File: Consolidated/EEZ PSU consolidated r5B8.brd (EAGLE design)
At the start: 316 x 150 mm, 529 parts, among them IC1 LTC3864, IC10 REF5025, IC11 DAC8552, IC12 ADG465SOT-23, IC13 TS5A9411DCKT, IC14 ADS1120, IC15 LP339D, IC16 LM25575, IC17 MC7812, IC18 TPD4E002DRLR, IC19 TPD2E001DZDR, IC2 MC79L05, IC20 ADUM3160BRWZ, IC21 TLC5925IDBQR, IC22 Si8641EC-B-IS1, IC23 SI8651EC-B-IS1, IC24 SI8651EC-B-IS1, IC25 LD1117ADT33TR, IC26 Si8641EC-B-IS1, IC27 PCA21125, IC28 AT25256B, IC29 W5500, IC3 MC78L05, IC30 BC857BS, IC31 TLC555, IC32 SN74LVC2G08DCTR, IC33 TPS3705-33D, IC34 SN74LV1T34DBVR, IC35 SN74LVC2G02DCTR, IC4 LM5574, IC5 LP2951SO8, IC6 TL072D, IC7 TL072D, IC8 OP27GSZ, IC9 MCP23S08-E/SO, J1 BS-244DSM-R, J2 BS-244DSM-G, J3 BS-244DSM-B, J4 BS-244DSM-R, J5 BS-244DSM-B, Q1 SUD19P06-60, Q10 MMBT5401, Q11 MMBT5401, Q12 MMBT5551, Q13 MMBT5551, Q14 BSS84P, Q15 2N7002, Q16 MMBT5551, Q17 MMBT5401, Q18 MMBT5551, Q19 MMBT5551, Q2 MMBT5401, Q20 BTA26-600, Q21 BTA26-600, Q22 IRLL014N, Q23 IRLML2246TRPBF, Q24 IRLML2246TRPBF, Q25 IRLML2246TRPBF, Q26 IRLML2246TRPBF, Q27 2N7002, Q28 IRLML2246TRPBF, Q29 2N7002, Q3 2N7002, Q30 2N7002, Q4 IRFP250N, Q5 BC857C, Q6 BC846C, Q7 BCP56-16.115, Q8 IRFR5410, Q9 BCP56-16.115, SW1 A101SYCQ04, SW2 1301.9316, X1 282836-3, X10 826629-5, X11 2411-01, X12 MC000006, X13 TSW-113-07-F-D, X14 MC000005, X15 TSW-113-07-F-D, X16 09185067324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

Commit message: Consolidated PCB, jumpers renumbering
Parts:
- removed JMP1, JMP2: 0R-JUMPA, jump-0r-smd:A0R-JMP
- added JP6, JP7: 0R-JUMPA, jump-0r-smd:A0R-JMP
- C18: value EEEFK1J470P -> EEEFK1J101P
- D28: device diode:DO214AC -> EEZ_Lib1:SOD123
- FB6, FB7: value 2506033007Y3 -> 60R@100MHz
- JP1: value 826926-2 -> 0R-JUMPA; device jumper:JP1 -> jump-0r-smd:A0R-JMP
- JP3: value 0R-JUMPA -> 826926-2; device jump-0r-smd:A0R-JMP -> jumper:JP1
- L2: value See Note 1.2 -> 7443551331
- LED1: device led:CHIPLED_0805 -> EEZ_Lib1:LED_0805
- R12: value See Note 1.3 -> 324K
- moved JP2 301.9 mm to (15.5, 134.0), turned to 90 degrees
- moved JP1 128.8 mm to (107.6, 125.8), turned to 180 degrees
- moved JP3 80.8 mm to (224.2, 71.1), turned to 90 degrees
- moved JP4 24.5 mm to (307.8, 58.8)
- moved JP5 12.2 mm to (299.5, 42.0)
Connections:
- net !INT: now also JP2.2; no longer JMP2.2
- net !PS_DRDY: now also JP2.3; no longer JMP2.3
- net !PWD_RST: now also JP3.1; no longer JP1.1
- net +3V3: now also JP4.3; no longer JP2.3
- net +5V: now also JP4.1; no longer JP2.1
- net GND: now also JP3.2; no longer JP1.2
- net INT_EXP: now also JP2.1; no longer JMP2.1
- net MISO: now also JP7.1; no longer JP5.1
- net MODE: now also JP1.2; no longer JMP1.2
- net MOSI: now also JP6.1; no longer JP4.1
- net N$102: now also JP4.2; no longer JP2.2
- net N$104: now also JP7.2; no longer JP5.2
- net N$105: now also JP5.2; no longer JP3.2
- net N$106: now also JP6.2; no longer JP4.2
- net SCLK: now also JP5.1; no longer JP3.1
- net SGND: now also JP1.1; no longer JMP1.1
- net SYNC: now also JP1.3; no longer JMP1.3
- net TOUCH_DIN: now also JP6.3; no longer JP4.3
- net TOUCH_DOUT: now also JP7.3; no longer JP5.3
- net TOUCH_SCLK: now also JP5.3; no longer JP3.3
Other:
- board text added: "JP6"
- board text added: "JP7"
- board text removed: "JMP1"
- board text removed: "JMP2"

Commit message: Fixed fan control, miniMELF replaced with SOD-323
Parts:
- added C157: 100n, rcl:C0603
- added D29: SKL16, EEZ_Lib1:SOD123
- C104: value 470n/100V -> 100n; device rcl:C1812 -> rcl:C0603
- C105, C110: value 10n -> 470n/100V; device rcl:C1206 -> rcl:C1812
- C106, C111: value UPW1J150MED -> 10n; device MyLib6:CAPAE660X610N_COMBO2 -> rcl:C1206
- C107: value 10u -> UPW1J150MED; device rcl:C1206 -> MyLib6:CAPAE660X610N_COMBO2
- C108: value 10n -> 10u
- C109: value 470n/100V -> 10n; device rcl:C1812 -> rcl:C1206
- C112: value 10n -> UPW1J150MED; device rcl:C1206 -> MyLib6:CAPAE660X610N_COMBO2
- C113: value 100n -> 10n; device rcl:C0603 -> rcl:C1206
- C119: value 47u -> 100n; device MyLib6:PANASONIC_C -> rcl:C0603
- C120: value 10u -> 47u
- C121: value 100n -> 10u; device rcl:C0603 -> MyLib6:PANASONIC_C
- C125: value 10u -> 100n; device rcl:C1206 -> rcl:C0603
- C126: value 100n -> 10u; device rcl:C0603 -> rcl:C1206
- C127: value EECS5R5H105 -> 100n; device EEZ_Lib1:SG-R20MM -> rcl:C0603
- C128: value 100n -> EECS5R5H105; device rcl:C0603 -> EEZ_Lib1:SG-R20MM
- C130: value 22n -> 100n; device rcl:C0805 -> rcl:C0603
- C131: value 18p -> 22n
- C132: value 6n8 -> 18p; device rcl:C0603 -> rcl:C0805
- C133: value 10n -> 6n8; device rcl:C0805 -> rcl:C0603
- C134: value 6n8 -> 10n; device rcl:C0603 -> rcl:C0805
- C135: value 18p -> 6n8; device rcl:C0805 -> rcl:C0603
- C136: value 100n -> 18p; device rcl:C0603 -> rcl:C0805
- C144: value 10u -> 100n; device EEZ_Lib1:EC1206 -> rcl:C0603
- C145: value 4u7 -> 10u
- C146: value 10n -> 4u7; device rcl:C0805 -> EEZ_Lib1:EC1206
- C147, C156: value 100n -> 10n; device rcl:C0603 -> rcl:C0805
- C148, C152: value 47n -> 100n; device rcl:C0805 -> rcl:C0603
- C149, C153, C99: value 100n -> 47n; device rcl:C0603 -> rcl:C0805
- C154: value 10n -> 100n; device rcl:C0805 -> rcl:C0603
- C97: value 100u -> 10u; device EEZ_Lib1:CAPAE660X610N -> MyLib6:PANASONIC_C
- C98: value 47n -> 100u; device rcl:C0805 -> EEZ_Lib1:CAPAE660X610N
- D25: value SMBJ5.0A-TR -> BAS316; device MyLib6:DO214AA -> diode:SOD323-W
- D26: value BAS316 -> SMBJ5.0A-TR; device diode:SOD323-W -> MyLib6:DO214AA
- D27: value BAT54S -> BAS316; device diode:SOT23 -> diode:SOD323-W
- D28: value SKL16 -> BAT54S; device EEZ_Lib1:SOD123 -> diode:SOT23
- ZD4: value 13V -> BZX384-C15.115; device EEZ_Lib1:MINIMELF -> EEZ_Lib1:SOD323-W
- ZD5: value 6V2 -> PDZ6.2B; device EEZ_Lib1:MINIMELF -> EEZ_Lib1:SOD323-W
- moved D25 192.5 mm to (119.5, 52.1), turned to 0 degrees
- moved C119 165.9 mm to (135.4, 61.0), turned to 90 degrees
- moved EEZ_SIGNATURE 128.8 mm to (3.81, 79.8)
- moved C104 125.8 mm to (68.7, 64.7)
- moved C123 119.6 mm to (152.7, 64.9)
- moved C121 116.6 mm to (260.0, 14.5), turned to 180 degrees
- moved D21 115.5 mm to (95.0, 65.3)
- moved C151 102.6 mm to (200.0, 67.6), turned to 180 degrees
- moved C113 93.7 mm to (125.4, 4.32), turned to 90 degrees
- moved C138 87.2 mm to (310.2, 31.8), turned to 0 degrees
- moved C117 85.0 mm to (211.1, 27.6), turned to 180 degrees
- moved D27 83.1 mm to (274.3, 49.2), turned to 270 degrees
- moved C150 81.1 mm to (270.3, 27.2), turned to 90 degrees
- moved C149 80.9 mm to (193.4, 52.3), turned to 0 degrees
- moved C154 73.4 mm to (312.0, 52.8), turned to 180 degrees
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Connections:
- new net N$163: D21.C, X6.3
- net !MR: now also C153.2; no longer C152.2
- net +3V3: now also C108.1, C116.1, C118.1, C121.1, C123.1, C127.1, C131.1, C137.2, C144.1, C145.+, C150.2, C151.1, C152.2, C154.1, C157.1, D27.A; no longer C107.1, C114.1, C117.1, C120.1, C122.1, C126.1, C130.1, C136.2, C138.1, C144.+, C149.2, C150.1, C151.2, C153.1, C156.1, D26.A
- net +5V: now also C100.1, C120.1, C126.2, D26.C; no longer C119.1, C125.2, C99.1, D25.C
- net 12VDC: now also C98.1
- net 1V2O: now also C147.2; no longer C146.2
- net AC_IN1: now also X2.1; no longer X2.2
- net AC_IN2: now also X2.2; no longer X2.1
- net AUX_FAN_SENSE: now also D21.A; no longer X6.3
- net CH1_GND: now also C114.2, C117.2, C148.2, C149.1; no longer C113.2, C116.2, C147.2, C148.1
- net CH1_VDD: now also C114.1, C117.1, C148.1; no longer C113.1, C116.1, C147.1
- net CH2_GND: now also C119.2, C122.2; no longer C118.2, C121.2
- net CH2_VDD: now also C119.1, C122.1; no longer C118.1, C121.1
- net DC+: now also L1.2; no longer L1.1
- net DC-: now also L1.1, X1.3; no longer L1.2, X1.1
- net DC_OUT: now also L1.3; no longer L1.4
- net EARTH: now also C106.2, C109.1, C111.2, C113.1, C131.2, C134.2, X1.1; no longer C105.2, C108.1, C110.2, C112.1, C130.2, C133.2, X1.3
- net ENC_A: now also C155.2, MCU.A8; no longer C154.2, MCU.A14
- net ENC_B: now also C156.1, MCU.A9; no longer C155.1, MCU.A15
- net ETH_IN+: now also C135.1; no longer C134.1
- net ETH_IN-: now also C133.1; no longer C132.1
- net FAN_OUT: now also C99.2; no longer C98.2
- net GND: now also C100.2, C103.2, C108.2, C116.2, C118.2, C121.2, C123.2, C126.1, C128.2, C130.1, C132.2, C136.2, C138.1, C144.2, C145.-, C147.1, C150.1, C151.2, C153.1, C154.2, C155.1, C157.2, C97.2, D26.A, D28.1, IC16.TP, L1.4; no longer C102.2, C107.2, C114.2, C117.2, C119.2, C122.2, C123.1, C126.2, C128.1, C131.2, C135.2, C136.1, C138.2, C144.-, C146.1, C149.1, C150.2, C151.1, C153.2, C154.1, C155.2, C99.2, D21.A, D27.1, L1.3
- net GNDA: now also C146.-; no longer C145.-
- net N$107: now also C128.1; no longer C127.1
- net N$109: now also C124.2, D27.C; no longer C123.2, D26.C
- net N$111: now also C132.1; no longer C131.1
- net N$112: now also C136.1; no longer C135.1
- net N$113: now also C133.2; no longer C132.2
- net N$115: now also C135.2; no longer C134.2
- net N$124: now also C134.1; no longer C133.1
- net N$132: now also C138.2; no longer C137.2
- net N$136: now also C149.2; no longer C148.2
- net N$139: now also D28.3; no longer D27.3
- net N$144: now also D28.2; no longer D27.2
- net N$148: now also D29.C; no longer D28.C
- net N$149: now also D29.A; no longer D28.A
- net N$155: now also D23.C; no longer D22.C
- net N$156: now also D24.C; no longer D23.C
- net N$84: now also C99.1; no longer C98.1
- net N$86: now also C98.2; no longer C97.2
- net N$87: now also C104.1; no longer C103.1
- net N$90: now also C101.1; no longer C100.1
- net N$91: now also C103.1; no longer C102.1
- net N$92: now also D22.C; no longer D21.C
- net N$93: now also D25.C; no longer D24.C
- net N$94: now also C105.2; no longer C104.2
- net N$95: now also C110.2; no longer C109.2
- net NTC1: now also C125.2; no longer C124.2
- net NTC2: now also C130.2; no longer C129.2
- net OUT1+: now also C106.1; no longer C105.1
- net OUT1-: now also C107.2, C107.2.1, C109.2; no longer C106.2, C106.2.1, C108.2
- net OUT2+: now also C112.1, C112.1.1; no longer C109.1, C111.1.1
- net OUT2-: now also C113.2; no longer C112.2
- net PWR_IN1+: now also C105.1, C107.1, C107.1.1; no longer C104.1, C106.1, C106.1.1
- net PWR_IN2-: now also C112.2, C112.2.1; no longer C111.2, C111.2.1
- net TEMP_ANALOG: now also C129.2; no longer C128.2
- net TOCAP: now also C146.+; no longer C145.+
- net XUSB_GND: now also C101.2, C102.1, C104.2; no longer C100.2, C101.1, C103.2
- net XUSB_VBUS: now also C102.2; no longer C101.2
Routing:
- net N$163: track 0.00 -> 30.0 mm
- net EARTH: track 239.5 -> 221.4 mm, vias 2 -> 1
- net AUX_FAN_SENSE: track 31.9 -> 19.8 mm
- net 12VDC: track 33.2 -> 43.9 mm
- net N$157: track 43.0 -> 35.5 mm
- net N$159: track 57.4 -> 49.8 mm
- net DC-: track 0.00 -> 6.15 mm
- net DC+: track 0.00 -> 6.15 mm
- net DC_OUT: track 84.2 -> 78.1 mm
- net +5V: track 899.9 -> 902.9 mm
- net ENC_A: track 10.0 -> 8.70 mm
- net GND: track 501.3 -> 500.0 mm, vias 276 -> 280
- net FAN_SENSE: track 78.0 -> 77.0 mm
- net +3V3: track 665.1 -> 665.7 mm, vias 53 -> 52
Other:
- board text added: "C157"
- board text added: "D29"
- board text added: "DC in max. 62V"
- board text removed: "DC in"
- board text removed: "max. 62V"

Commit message: Missed hole added to Power board, minor bottom silk mask changes
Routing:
- net EARTH: track 221.4 -> 243.3 mm, vias 1 -> 2

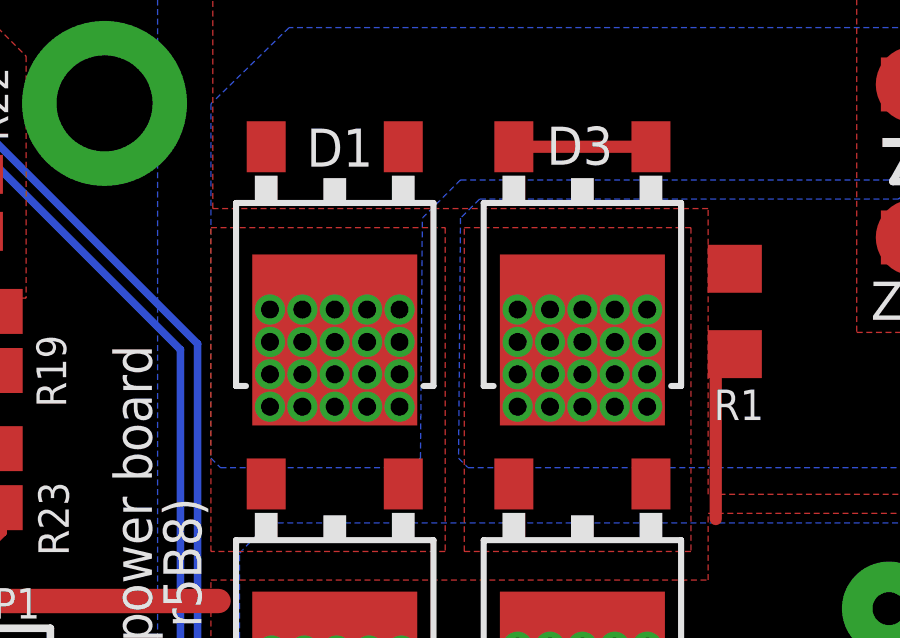
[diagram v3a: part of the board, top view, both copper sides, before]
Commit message: Consolidated BOM for PCBA, AUX PS BOM update, Power module PCB update
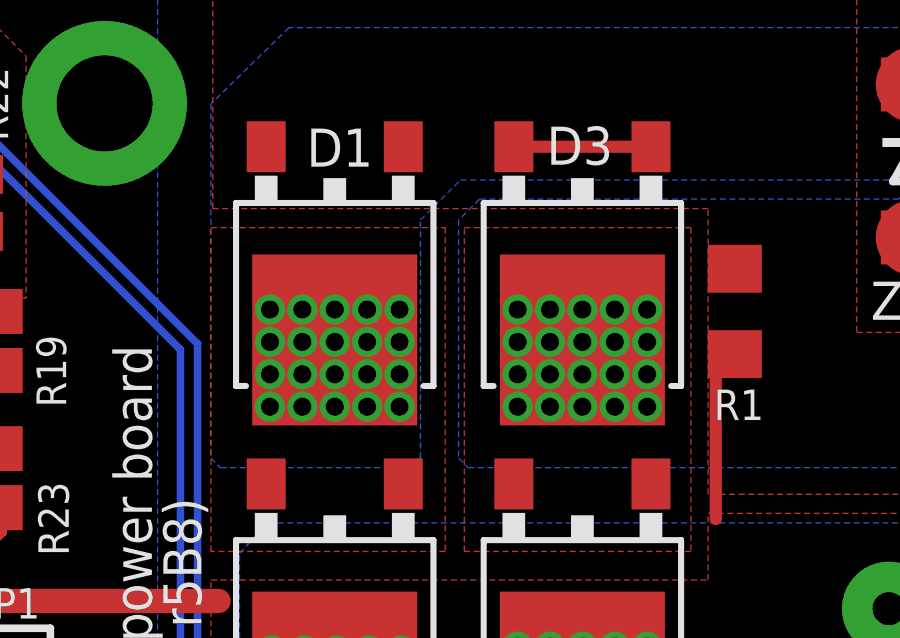
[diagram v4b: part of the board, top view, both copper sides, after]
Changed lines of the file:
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@@
 <vertex x="120.7135" y="133.858"/>
 <vertex x="121.031" y="134.1755"/>
-<vertex x="121.0945" y="142.1765"/>
+<vertex x="121.031" y="142.113"/>
 <vertex x="122.3645" y="143.4465"/>
 <vertex x="136.652" y="143.4465"/>
@@
 <vertex x="136.9695" y="142.8115"/>
 <vertex x="122.9995" y="142.8115"/>
-<vertex x="122.3645" y="142.1765"/>
+<vertex x="122.301" y="142.113"/>
 <vertex x="122.301" y="134.1755"/>
 <vertex x="122.6185" y="133.858"/>

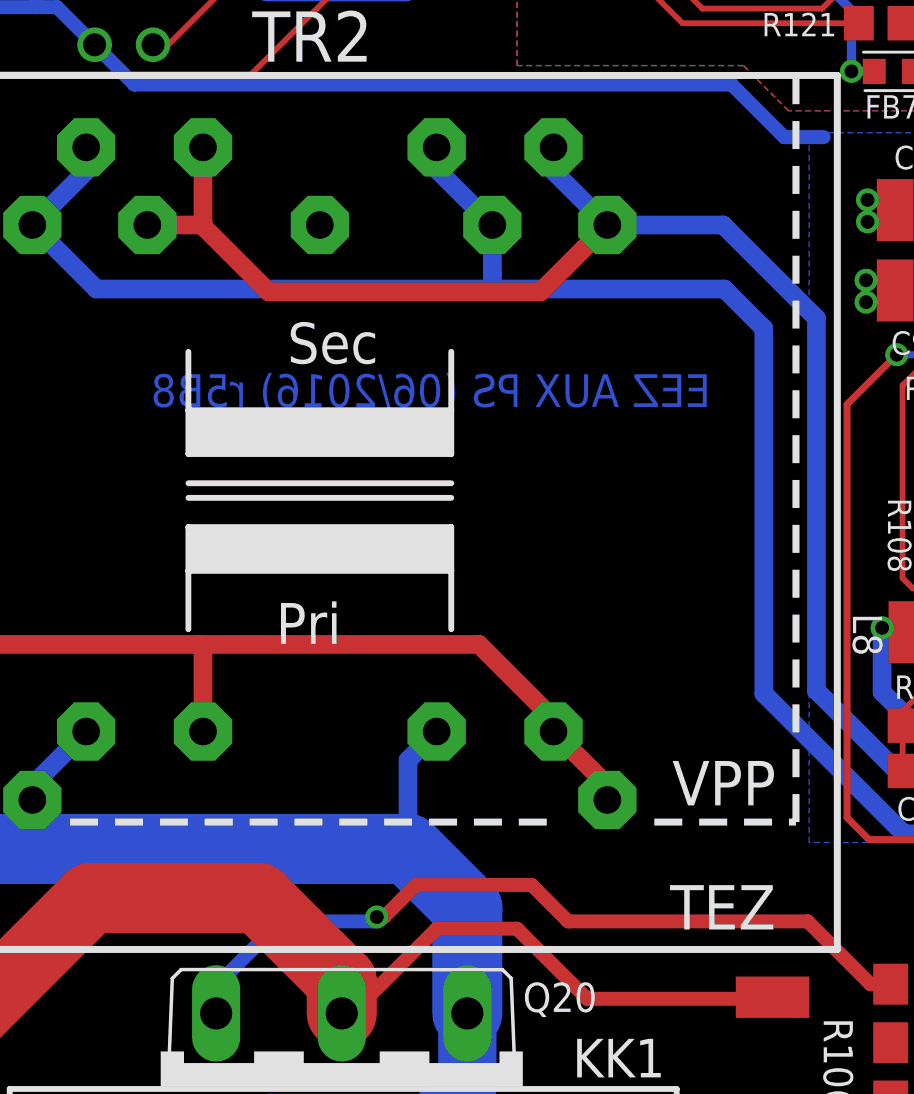
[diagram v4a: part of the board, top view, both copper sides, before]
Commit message: Myrra AC/DC module for 115VAC, BOM updated
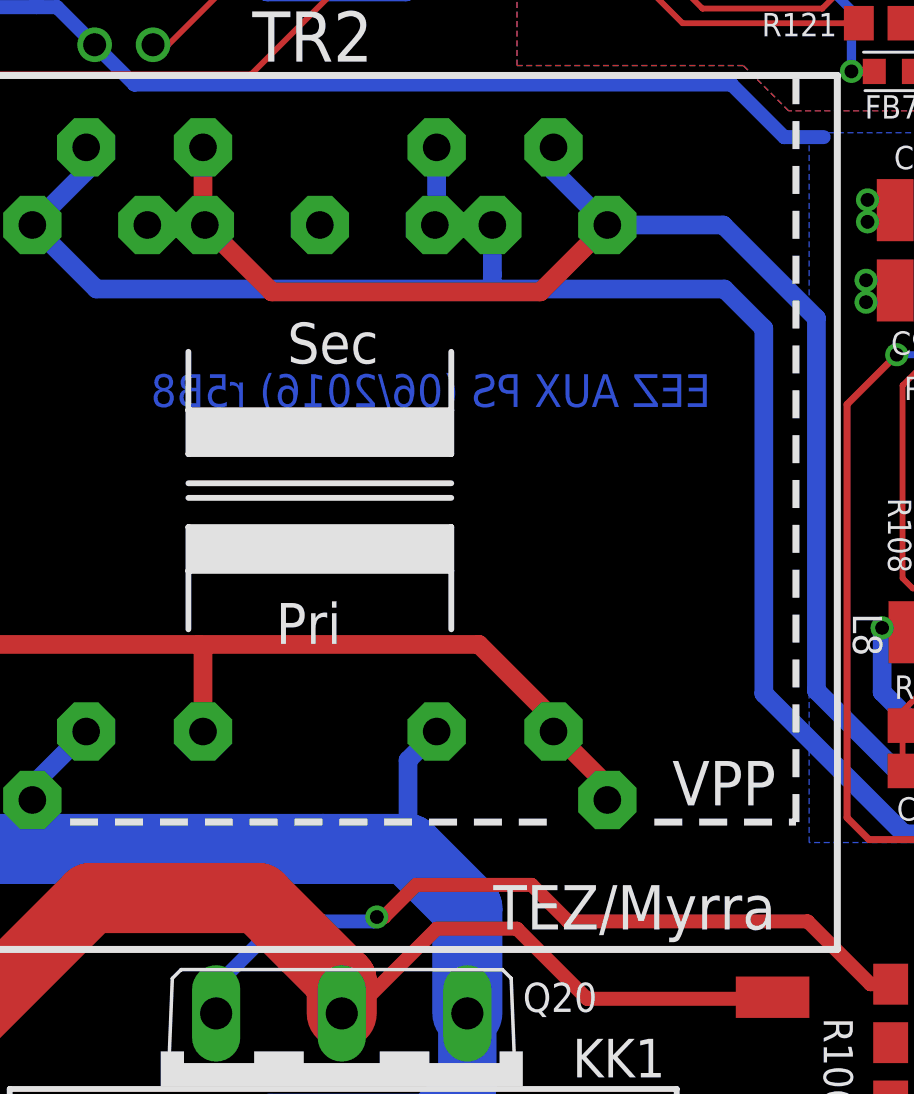
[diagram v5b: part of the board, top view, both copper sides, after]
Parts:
- TR2: device EEZ_Lib1:PCB_TRAFO6VA_TEZ+VPP -> EEZ_Lib1:PCB_TRAFO6VA_7.5W
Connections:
- net N$78: now also TR2.S2M
- net N$80: now also TR2.S1M
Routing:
- net N$80: track 102.2 -> 103.8 mm
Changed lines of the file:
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@@
 <element name="U$5" library="olimex_logo1" package="PB_SMALL" value="" x="92.9685" y="54.611" smashed="yes"/>
 <element name="U$6" library="olimex_logo1" package="ESD_SYMBOL" value="" x="86.456" y="57.1925" smashed="yes"/>
-<element name="TR2" library="EEZ_Lib1" package="PCB_TRAFO6VA_TEZ+VPP" value="TEZ6/D230/15V" x="45.085" y="37.719" smashed="yes" rot="R270">
-<attribute name="TME" value="TEZ6/D/15-15V" x="45.085" y="37.719" size="1.778" layer="27" rot="R270" display="off"/>
-<attribute name="MOUSER" value="553-VPP28-180" x="45.085" y="37.719" size="1.778" layer="27" rot="R270" display="off"/>
-<attribute name="NEWARK" value="37B9209" x="45.085" y="37.719" size="1.778" layer="27" rot="R270" display="off"/>
-<attribute name="DIGIKEY" value="237-1086-ND" x="45.085" y="37.719" size="1.778" layer="27" rot="R270" display="off"/>
+<element name="TR2" library="EEZ_Lib1" package="PCB_TRAFO6VA_7.5W" value="TEZ6/D230/15V" x="45.085" y="37.719" smashed="yes" rot="R270">
 <attribute name="NAME" x="42.1505" y="57.3195" size="2.1844" layer="25" ratio="10" rot="SR0"/>
 <attribute name="VALUE" x="33.324" y="36.7455" size="2.1844" layer="27" ratio="10"/>
@@
 <wire x1="81.2165" y1="21.844" x2="81.2165" y2="9.7155" width="0.8128" layer="16"/>
 <via x="89.154" y="1.778" extent="1-16" drill="0.7" shape="octagon"/>
-<wire x1="42.8625" y1="47.3075" x2="54.6735" y2="47.3075" width="0.8128" layer="1"/>
-<wire x1="37.585" y1="50.219" x2="39.9415" y2="50.219" width="0.8128" layer="1"/>
-<wire x1="39.9415" y1="50.219" x2="39.951" y2="50.219" width="0.8128" layer="1"/>
-<wire x1="39.951" y1="50.219" x2="42.8625" y2="47.3075" width="0.8128" layer="1"/>
-<wire x1="40.005" y1="53.594" x2="40.005" y2="50.2825" width="0.8128" layer="1"/>
-<wire x1="40.005" y1="50.2825" x2="39.9415" y2="50.219" width="0.8128" layer="1"/>
+<wire x1="42.9965" y1="47.3075" x2="54.6735" y2="47.3075" width="0.8128" layer="1"/>
 <wire x1="54.6735" y1="47.3075" x2="57.585" y2="50.219" width="0.8128" layer="1"/>
 <wire x1="55.245" y1="53.594" x2="55.245" y2="52.559" width="0.8128" layer="16"/>
@@
 <wire x1="89.7805" y1="1.7865" x2="89.154" y2="1.778" width="0.8128" layer="1"/>
 <wire x1="81.2165" y1="9.7155" x2="89.154" y2="1.778" width="0.8128" layer="16"/>
+<contactref element="TR2" pad="S2M"/>
+<wire x1="42.9965" y1="47.3075" x2="40.085" y2="50.219" width="0.8128" layer="1"/>
+<wire x1="40.005" y1="53.594" x2="40.005" y2="50.299" width="0.8128" layer="1"/>
+<wire x1="40.005" y1="50.299" x2="40.085" y2="50.219" width="0.8128" layer="1"/>
+<wire x1="37.585" y1="50.219" x2="40.085" y2="50.219" width="0.8128" layer="1"/>
 </signal>
 <signal name="N$80">
@@
 <wire x1="34.925" y1="53.594" x2="34.925" y2="52.559" width="0.8128" layer="16"/>
 <wire x1="34.925" y1="52.559" x2="32.585" y2="50.219" width="0.8128" layer="16"/>
-<wire x1="50.165" y1="53.594" x2="50.165" y2="52.639" width="0.8128" layer="16"/>
-<wire x1="50.165" y1="52.639" x2="52.585" y2="50.219" width="0.8128" layer="16"/>
 <wire x1="52.585" y1="50.219" x2="52.585" y2="48.0765" width="0.8128" layer="16"/>
 <wire x1="52.585" y1="48.0765" x2="52.578" y2="47.4345" width="0.8128" layer="16"/>
@@
 <wire x1="84.51" y1="1.7865" x2="84.074" y2="1.778" width="0.8128" layer="1"/>
 <wire x1="79.375" y1="6.477" x2="84.074" y2="1.778" width="0.8128" layer="16"/>
+<contactref element="TR2" pad="S1M"/>
+<wire x1="50.085" y1="50.219" x2="50.165" y2="50.219" width="0.8128" layer="16"/>
+<wire x1="50.165" y1="50.219" x2="50.165" y2="53.594" width="0.8128" layer="16"/>
+<wire x1="52.585" y1="50.219" x2="50.085" y2="50.219" width="0.8128" layer="16"/>
 </signal>
 <signal name="TA5">

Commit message: PCB fiducials, outlines, milling bridges
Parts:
- added U$11, U$12, U$13, U$14, U$15, U$16: FIDUCIAL_2, EEZ_Lib1:FIDUCIAL_DUAL
- moved EEZ_SIGNATURE 66.4 mm to (3.81, 146.3)
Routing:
- net WIFI_CE: track 54.2 -> 53.5 mm
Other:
- board text removed: "*"
- board text removed: "* Check instructions for R13 installation"
